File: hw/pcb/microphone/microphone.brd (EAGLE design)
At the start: 160 x 100 mm, 0 parts

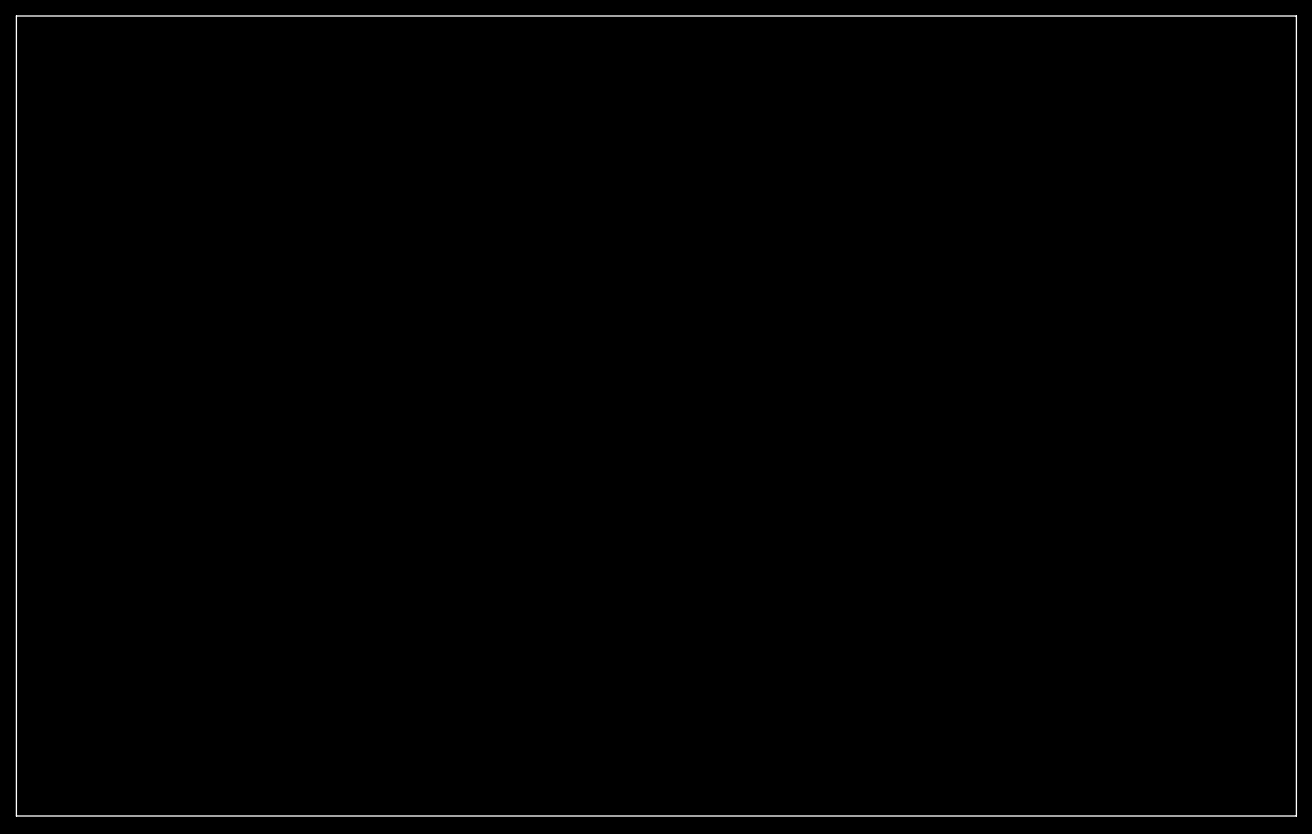
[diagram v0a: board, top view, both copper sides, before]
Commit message: Add microphone board
Completed schematic and layout of microphone board. Is a similar
design to the one from TI's tidu765 app-note. Has provisions for a
more basic non-inverting amplifier design as well. Currently uses a
transimpedence amplifier.
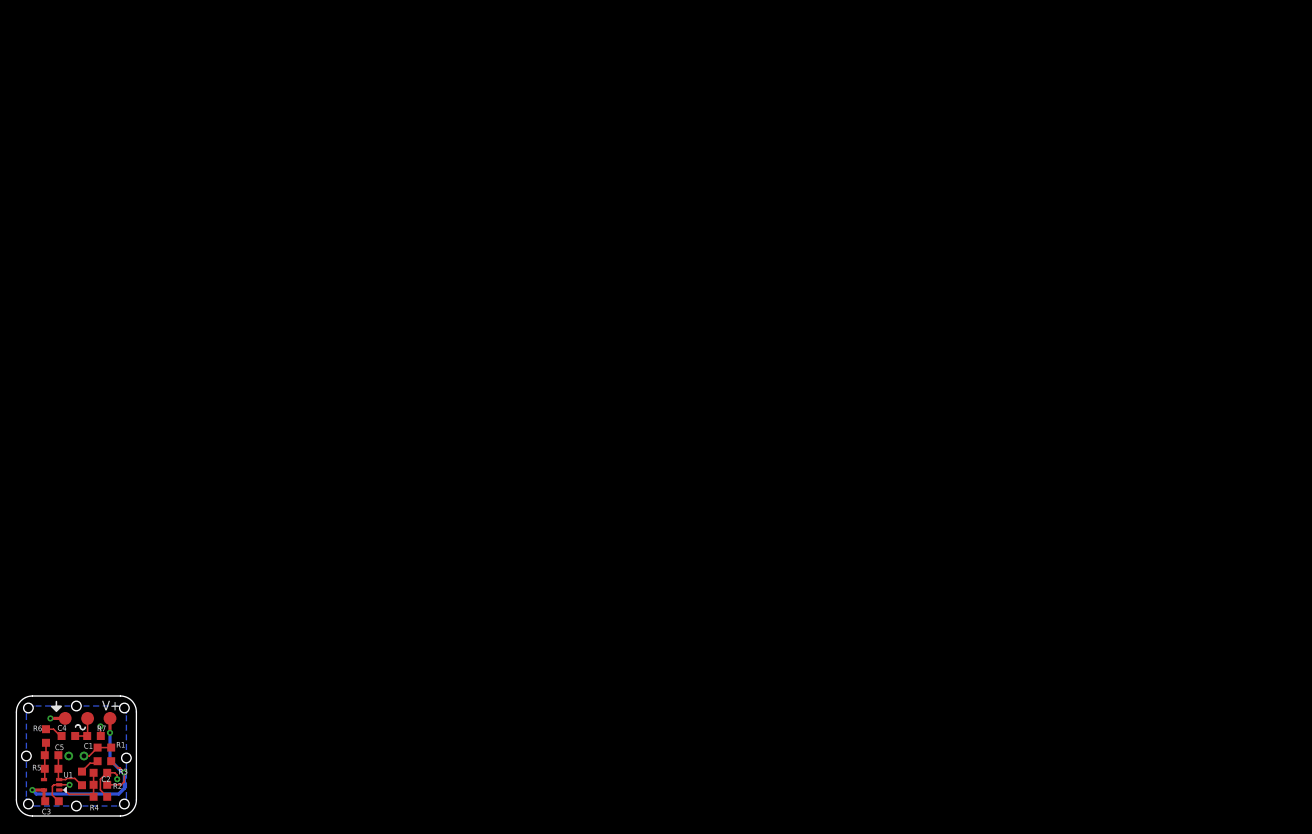
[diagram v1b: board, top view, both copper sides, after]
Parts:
- added C1, C2, C3, C4, C5: (no value), wedfestdress:CAP_0603
- added MIC1: (no value), wedfestdress:POM-5238P-R
- added R1, R2, R3, R4, R5, R6, R7: (no value), wedfestdress:RES_0603
- added TP1, TP2, TP3: (no value), wedfestdress:TP_1P6_MM_ROUND
- added U1: (no value), wedfestdress:SC-70-5_GENERIC
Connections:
- new net 3V3: C3.P$1, R1.P$2, R2.P$2, TP1.P$1, U1.5
- new net AMP_NEG: C5.P$1, R4.P$2, R5.P$1, U1.3
- new net AMP_OUT: C5.P$2, R5.P$2, R6.P$1, U1.4
- new net AMP_OUT_R: C4.P$1, R6.P$2
- new net GND: C2.P$1, C3.P$2, MIC1.NEG, R3.P$1, R7.P$1, TP3.P$1, U1.2
- new net MIC_OUT: C1.P$1, MIC1.POS, R1.P$1
- new net MIC_OUT_C: C1.P$2, R4.P$1
- new net REF: C2.P$2, R2.P$1, R3.P$2, U1.1
- new net SIGNAL_OUT: C4.P$2, R7.P$2, TP2.P$1
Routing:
- net 3V3: track 0.00 -> 30.4 mm, vias 0 -> 3
- net GND: track 0.00 -> 13.6 mm, vias 0 -> 4
- net REF: track 0.00 -> 7.65 mm
- net AMP_NEG: track 0.00 -> 6.36 mm
- net AMP_OUT: track 0.00 -> 4.70 mm
- net SIGNAL_OUT: track 0.00 -> 3.93 mm
- net MIC_OUT: track 0.00 -> 3.83 mm
- net MIC_OUT_C: track 0.00 -> 2.52 mm
- net AMP_OUT_R: track 0.00 -> 2.30 mm
- added copper zone on layer 16, net GND
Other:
- board size 160 x 100 mm -> 15 x 15 mm
- board text added: "Rev A"
- board text added: "V+"
- board text added: "Wedfestdress Mic"

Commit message: Final tweaks and CAM output for all three boards
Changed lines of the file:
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@@
 <layer number="27" name="tValues" color="7" fill="1" visible="no" active="yes"/>
 <layer number="28" name="bValues" color="7" fill="1" visible="no" active="yes"/>
-<layer number="29" name="tStop" color="7" fill="3" visible="no" active="yes"/>
-<layer number="30" name="bStop" color="7" fill="6" visible="no" active="yes"/>
-<layer number="31" name="tCream" color="7" fill="4" visible="no" active="yes"/>
-<layer number="32" name="bCream" color="7" fill="5" visible="no" active="yes"/>
+<layer number="29" name="tStop" color="7" fill="3" visible="yes" active="yes"/>
+<layer number="30" name="bStop" color="7" fill="6" visible="yes" active="yes"/>
+<layer number="31" name="tCream" color="7" fill="4" visible="yes" active="yes"/>
+<layer number="32" name="bCream" color="7" fill="5" visible="yes" active="yes"/>
 <layer number="33" name="tFinish" color="6" fill="3" visible="no" active="yes"/>
 <layer number="34" name="bFinish" color="6" fill="6" visible="no" active="yes"/>
@@
 <attribute name="NOSTUFF" value="" x="11.85" y="7.7" size="0.9" layer="27" ratio="10" rot="R270" display="off"/>
 <attribute name="COST_X500" value=".00514" x="11.85" y="7.7" size="0.9" layer="27" ratio="10" rot="R270" display="off"/>
-<attribute name="NAME" x="12.47" y="8.55" size="0.7" layer="21" font="vector"/>
+<attribute name="NAME" x="12.67" y="8.45" size="0.7" layer="21" font="vector"/>
 <attribute name="NAME" x="10.85" y="6.43" size="1" layer="105" font="vector" rot="R270"/>
 </element>
@@
 <attribute name="NOSTUFF" value="" x="10.5" y="5.4" size="0.9" layer="27" ratio="10" rot="R180" display="off"/>
 <attribute name="COST_X500" value=".00382" x="10.5" y="5.4" size="0.9" layer="27" ratio="10" rot="R180" display="off"/>
-<attribute name="NAME" x="13.93" y="5.9" size="0.7" layer="21" font="vector" rot="R180"/>
+<attribute name="NAME" x="13.33" y="5.8" size="0.7" layer="21" font="vector" rot="R180"/>
 <attribute name="NAME" x="9.23" y="6.4" size="1" layer="105" font="vector" rot="R180"/>
 </element>
@@
 <attribute name="NOSTUFF" value="" x="10.5" y="2.4" size="0.9" layer="27" ratio="10" rot="R180" display="off"/>
 <attribute name="COST_X500" value="0.06626" x="10.5" y="2.4" size="0.9" layer="27" ratio="10" rot="R180" display="off"/>
-<attribute name="NAME" x="11.77" y="4.94" size="0.7" layer="21" font="vector" rot="R180"/>
+<attribute name="NAME" x="10.37" y="1.64" size="0.7" layer="21" font="vector" rot="R180"/>
 </element>
 <element name="C3" library="wedfestdress" package="CAP_0603" value="" x="4.45" y="1.85" smashed="yes">
@@
 <attribute name="NOSTUFF" value="" x="4.45" y="1.85" size="0.9" layer="27" ratio="10" display="off"/>
 <attribute name="COST_X500" value="0.0154" x="4.45" y="1.85" size="0.9" layer="27" ratio="10" display="off"/>
-<attribute name="NAME" x="3.18" y="0.21" size="0.7" layer="21" font="vector"/>
+<attribute name="NAME" x="3.18" y="0.41" size="0.7" layer="21" font="vector"/>
 </element>
 <element name="R4" library="wedfestdress" package="RES_0603" value="" x="8.2" y="4.7" smashed="yes" rot="R270">
@@
 <attribute name="NOSTUFF" value="" x="8.2" y="4.7" size="0.9" layer="27" ratio="10" rot="R270" display="off"/>
 <attribute name="COST_X500" value="0.00278" x="8.2" y="4.7" size="0.9" layer="27" ratio="10" rot="R270" display="off"/>
-<attribute name="NAME" x="9.17" y="0.7" size="0.7" layer="21" font="vector"/>
+<attribute name="NAME" x="6.87" y="6.2" size="0.7" layer="21" font="vector"/>
 <attribute name="NAME" x="7.2" y="3.43" size="1" layer="105" font="vector" rot="R270"/>
 </element>
@@
 <attribute name="NOSTUFF" value="" x="4.4" y="5.9" size="0.9" layer="27" ratio="10" rot="R180" display="off"/>
 <attribute name="COST_X500" value=".006" x="4.4" y="5.9" size="0.9" layer="27" ratio="10" rot="R180" display="off"/>
-<attribute name="NAME" x="3.13" y="6.4" size="0.7" layer="21" font="vector" rot="R180"/>
+<attribute name="NAME" x="3.03" y="6.3" size="0.7" layer="21" font="vector" rot="R180"/>
 <attribute name="NAME" x="3.13" y="6.9" size="1" layer="105" font="vector" rot="R180"/>
 </element>
@@
 <attribute name="NOSTUFF" value="" x="9.7" y="10" size="0.9" layer="27" ratio="10" rot="R180" display="off"/>
 <attribute name="COST_X500" value=".00316" x="9.7" y="10" size="0.9" layer="27" ratio="10" rot="R180" display="off"/>
-<attribute name="NAME" x="11.23" y="11.3" size="0.7" layer="21" font="vector" rot="R180"/>
+<attribute name="NAME" x="11.33" y="11.4" size="0.7" layer="21" font="vector" rot="R180"/>
 <attribute name="NAME" x="8.43" y="11" size="1" layer="105" font="vector" rot="R180"/>
 </element>
